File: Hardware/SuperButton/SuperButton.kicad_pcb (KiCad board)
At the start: 2 copper layers, 53 x 53 mm, 28 parts, among them J101 USBC, J102 EXT_LED, J103 ICSP, SW101 Switch, U101 ATmega8U2-A, U102 ATtiny85

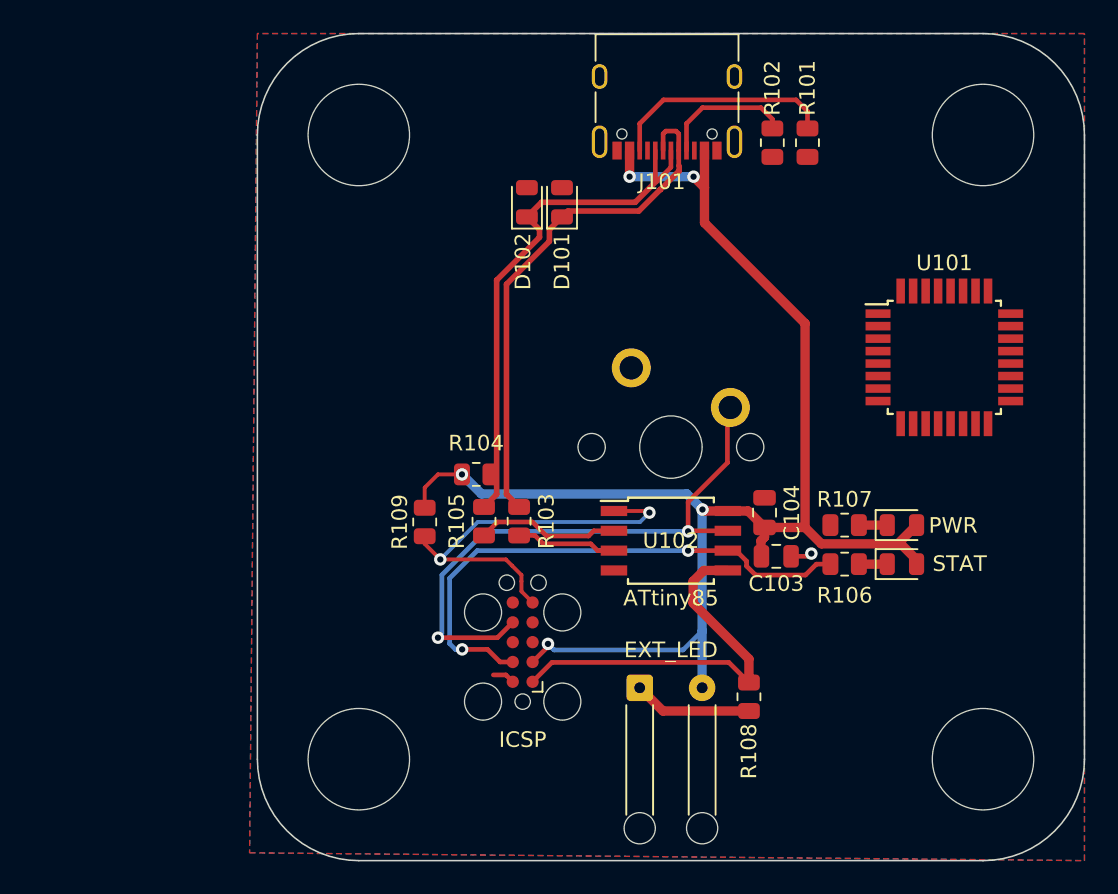
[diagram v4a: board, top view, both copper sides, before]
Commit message: Finalize inital button design
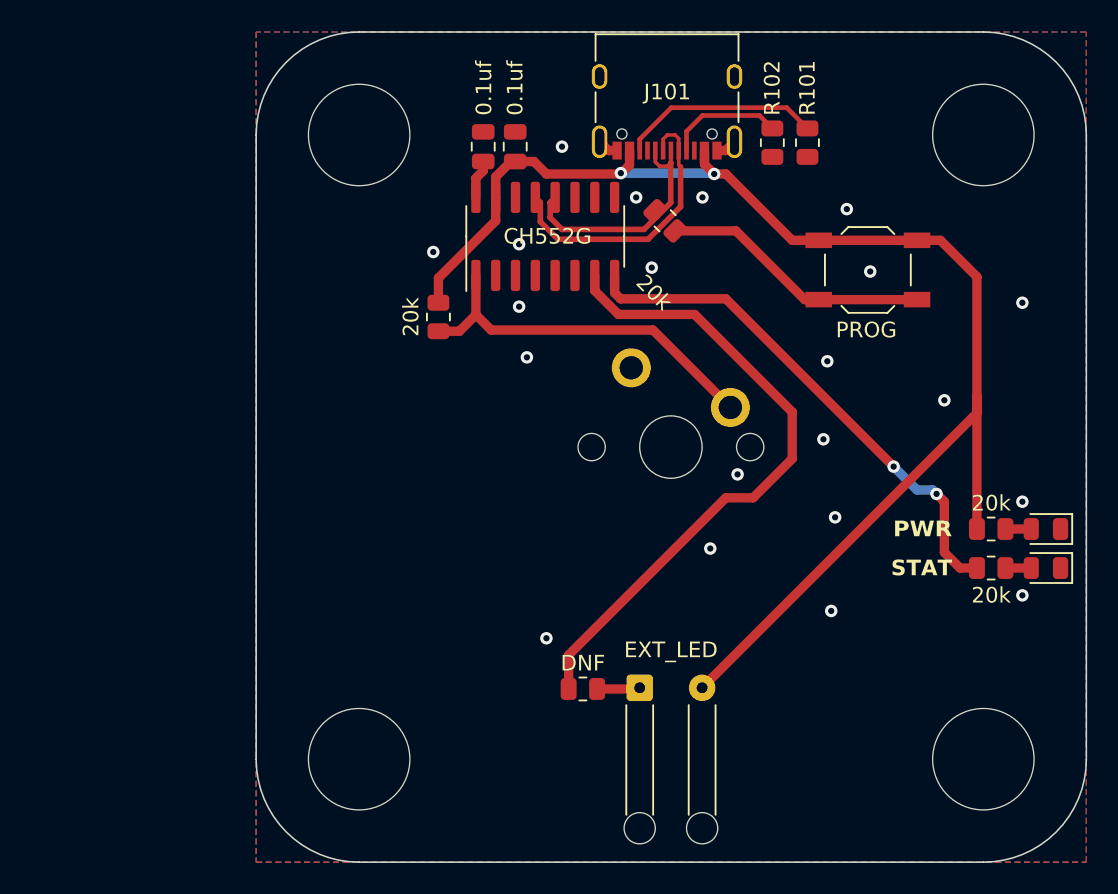
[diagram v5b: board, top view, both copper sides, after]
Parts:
- removed C103: 5pf, Capacitor_SMD:C_0805_2012Metric
- removed D101, D102: 3.6 Zener, Diode_SMD:D_0805_2012Metric
- removed J103: ICSP, Connector:Tag-Connect_TC2050-IDC-FP_2x05_P1.27mm_Vertical
- removed R107, R109: 1K, Resistor_SMD:R_0805_2012Metric
- removed U102: ATtiny85, Package_SO:SOIC-8W_5.3x5.3mm_P1.27mm
- added C101: 0.1uf, Capacitor_SMD:C_0805_2012Metric, F.Cu at (159.9, 70.8)
- added REF**: KiCad-Logo2_5mm_SilkScreen, Symbol:KiCad-Logo2_5mm_SilkScreen, B.Cu at (153.8, 92.8)
- added SW102: PROG, Button_Switch_SMD:SW_SPST_TL3342, F.Cu at (184.6, 78.7)
- R103, R105: value 68R -> 20k
- R104: value 1K5 -> 20k
- R106: value 1K -> 20k
- R108: value 1K -> DNF
- U101: value ATmega8U2-A -> CH552G; footprint Package_QFP:TQFP-32_7x7mm_P0.8mm -> Package_SO:SOP-16_3.9x9.9mm_P1.27mm
- moved R103 30.3 mm to (192.5, 95.2), turned to 180 degrees
- moved C104 28.4 mm to (162.0, 70.8)
- moved U101 26.7 mm to (163.9, 76.5), turned to 90 degrees
- moved R104 20.3 mm to (171.6, 75.5), turned to 135 degrees
- moved G*** 18.8 mm to (163.2, 110.0)
- moved R105 13.4 mm to (157.1, 81.7), turned to 90 degrees
- moved R108 10.7 mm to (166.3, 105.5), turned to 180 degrees
- moved R106 9.39 mm to (192.5, 97.8), turned to 180 degrees
- moved D103 9.23 mm to (196.0, 97.8), turned to 180 degrees
- moved D104 9.23 mm to (196.0, 95.2), turned to 180 degrees
- turned H104 to -90 degrees
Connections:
- D103 pad 1: Net-(D103-Pad1) -> GND
- D103 pad 2: +5V -> Net-(D103-A)
- D104 pad 1: Net-(D104-Pad1) -> GND
- D104 pad 2: +5V -> Net-(D104-A)
- R103 pad 1: /USB- -> Net-(D104-A)
- R103 pad 2: /USBB -> +5V
- R104 pad 1: +5V -> Net-(R104-Pad1)
- R105 pad 1: /USB+ -> /SW_SENSE
- R105 pad 2: /USBA -> +5V
- R106 pad 1: /SDI -> Net-(D103-A)
- R106 pad 2: Net-(D103-Pad1) -> /STAT
- R108 pad 2: /SDO -> /EXT
- SW101 pad 1: /SCK -> /SW_SENSE
- U101 pad 1: unconnected-(U101-Pad1) -> /SW_SENSE
- U101 pad 12: unconnected-(U101-Pad12) -> /USB+
- U101 pad 13: unconnected-(U101-Pad13) -> /USB-
- U101 pad 14: unconnected-(U101-Pad14) -> GND
- U101 pad 15: unconnected-(U101-Pad15) -> +5V
- U101 pad 16: unconnected-(U101-Pad16) -> +3V3
- U101 pad 6: unconnected-(U101-Pad6) -> /RST
- U101 pad 7: unconnected-(U101-Pad7) -> /EXT
- U101 pad 8: unconnected-(U101-Pad8) -> /STAT
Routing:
- net /EXT: track 0.00 -> 41.6 mm
- net /SCK: track 37.9 -> 0.00 mm, vias 2 -> 0
- net /SDI: track 35.0 -> 0.00 mm, vias 2 -> 0
- net /STAT: track 0.00 -> 33.5 mm, vias 0 -> 2
- net /RST: track 26.5 -> 0.00 mm, vias 2 -> 0
- net /SDO: track 25.7 -> 0.00 mm
- net /SW_SENSE: track 0.00 -> 24.1 mm
- net /USB+: track 34.0 -> 15.8 mm
- net Net-(R104-Pad1): track 0.00 -> 17.3 mm
- net /USB-: track 33.7 -> 18.4 mm
- net /USBA: track 9.20 -> 0.00 mm
- net /USBB: track 6.48 -> 0.00 mm
- net +5V: track 96.5 -> 90.7 mm, vias 5 -> 2
- net Net-(J102-Pin_1): track 7.62 -> 2.65 mm
- net +3V3: track 0.00 -> 2.49 mm
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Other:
- board size 53 x 53 mm -> 53.2 x 53.2 mm
- board text added: "Find programming resources here!"

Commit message: fixups
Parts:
- removed J102: EXT_LED, Connector_Wire:SolderWire-0.15sqmm_1x02_P4mm_D0.5mm_OD1.5mm_Relief
- added J103: EXT_LED, Connector_Wire:SolderWire-0.15sqmm_1x02_P4mm_D0.5mm_OD1.5mm_Relief, F.Cu at (170.0, 105.4)
- added TP101: TestPoint, TestPoint:TestPoint_Pad_2.5x2.5mm, B.Cu at (165.8, 80.4)
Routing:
- net /RST: track 0.00 -> 1.41 mm, vias 0 -> 1
